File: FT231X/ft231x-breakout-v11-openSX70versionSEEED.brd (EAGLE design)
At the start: 31.8 x 15.2 mm, 24 parts, among them J1 XF2L-0625-1, Q1 2N7002, U1 FTS31XS-U

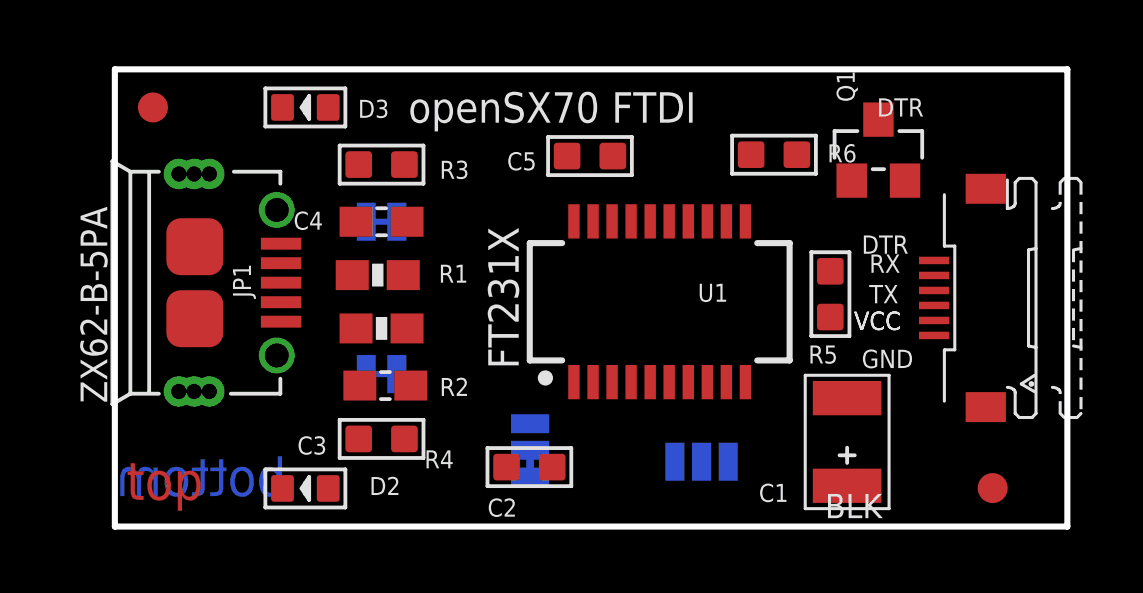
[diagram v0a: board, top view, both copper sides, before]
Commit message: NEW FTDI for manufacture 232RL based on Sparkfun FTDI basic
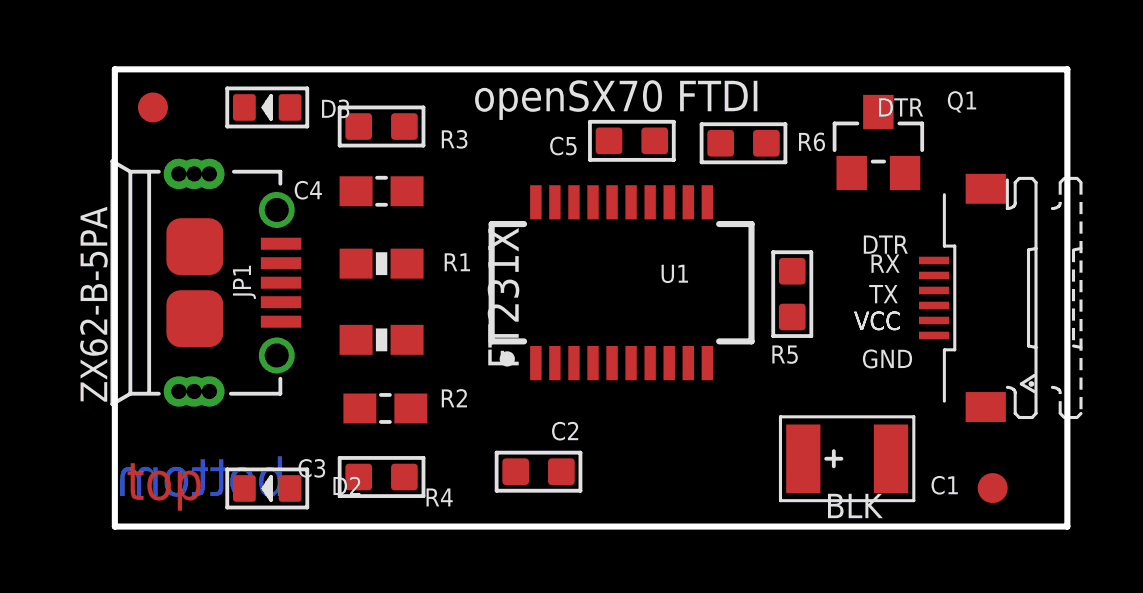
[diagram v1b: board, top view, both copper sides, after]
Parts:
- removed SJ1, SJ4: (no value), SparkFun-Passives:SJ_3
- removed SJ2: TXLED, SparkFun-Passives:SJ_2S-TRACE
- removed SJ3: RXLED, SparkFun-Passives:PAD-JUMPER-2-NC_BY_TRACE_YES_SILK
- moved C5 1.49 mm to (17.2, 12.9)
- moved U1 1.42 mm to (16.9, 8.13)
- moved R3 1.27 mm to (8.89, 13.3)
- moved R4 1.27 mm to (8.89, 1.65)
- moved D2 1.27 mm to (5.08, 1.27)
- moved D3 1.27 mm to (5.08, 14.0)
- moved R5 1.27 mm to (22.6, 7.75)
- moved R6 1.09 mm to (21.0, 12.8)
- moved C4 1.02 mm to (8.89, 11.2)
- moved C3 0.76 mm to (9.02, 3.94)
- moved C1 0.56 mm to (24.4, 2.26), turned to 0 degrees
- moved R1 0.40 mm to (8.89, 8.76)
- moved R2 0.38 mm to (8.89, 6.22)
- moved C2 0.34 mm to (14.1, 1.83), turned to 270 degrees
- moved Q1 0.25 mm to (25.5, 12.8)
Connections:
- removed net N$10: J1.3, SJ4.2
- removed net N$7: R3.1, SJ2.2
- removed net N$8: R4.1, SJ3.2
- net 3.3V: no longer SJ1.1
- net RXLED: now also R4.1; no longer SJ3.1
- net TXLED: now also R3.1; no longer SJ2.1
- net VCC: no longer SJ1.3
- net VOUT: now also J1.3; no longer SJ1.2, SJ4.3
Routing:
- net N$9: track 0.76 -> 0.00 mm
